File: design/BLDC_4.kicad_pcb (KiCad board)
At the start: 4 copper layers, 38.5 x 65 mm, 127 parts, among them K1 SERVO, P1 HALL/Encoder, P101 CANBUS, P2 SWD, P3 PWR_COMM, P4 IN+, P5 IN-, P6 MOTOR1, P7 MOTOR2, P9 MOTOR3, Q1 IRFS7530, Q2 IRFS7530, Q3 IRFS7530, Q4 IRFS7530, Q5 IRFS7530, Q6 IRFS7530, U1 STM32F40X_LQFP64, U2 TC2117, U3 DRV8302, U401 SN65HVD232, X1 MINI-USB-SHIELD-32005-201, X2 8MHz 10ppm

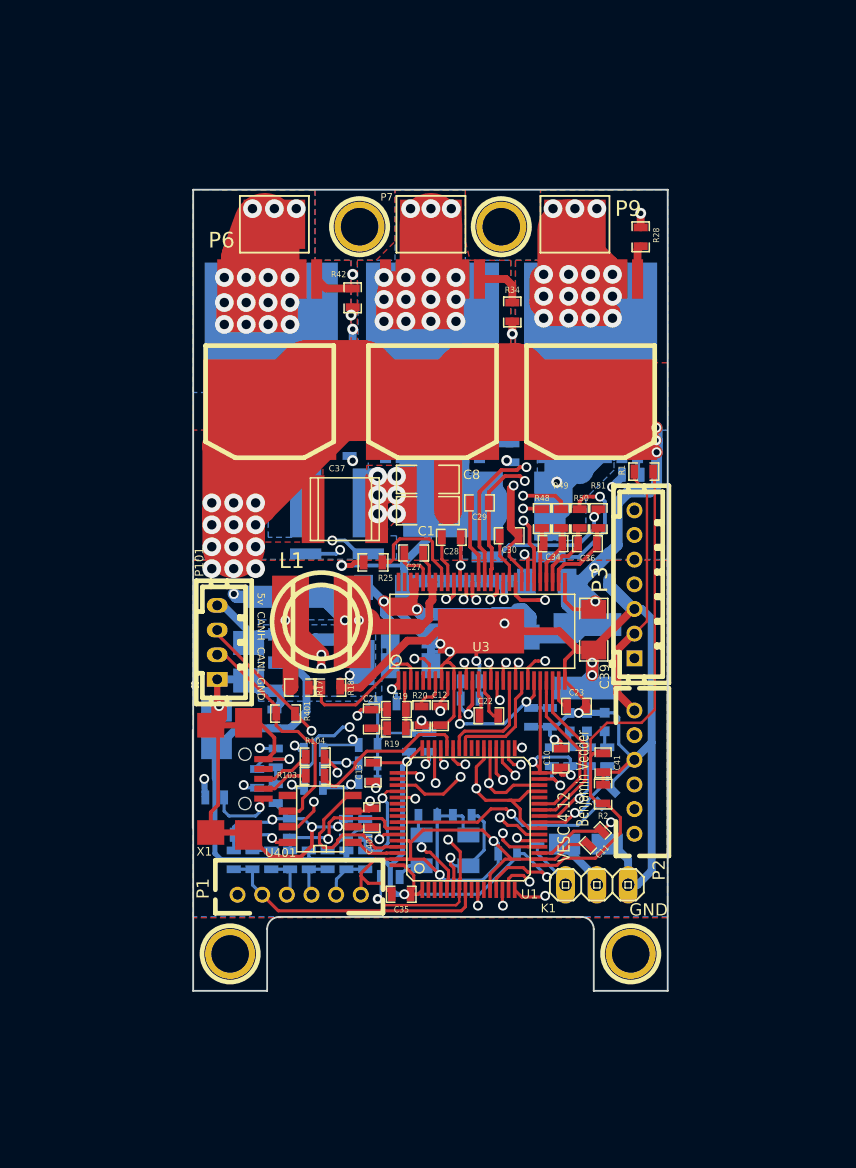
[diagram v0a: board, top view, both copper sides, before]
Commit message: Going to KiCAD 6
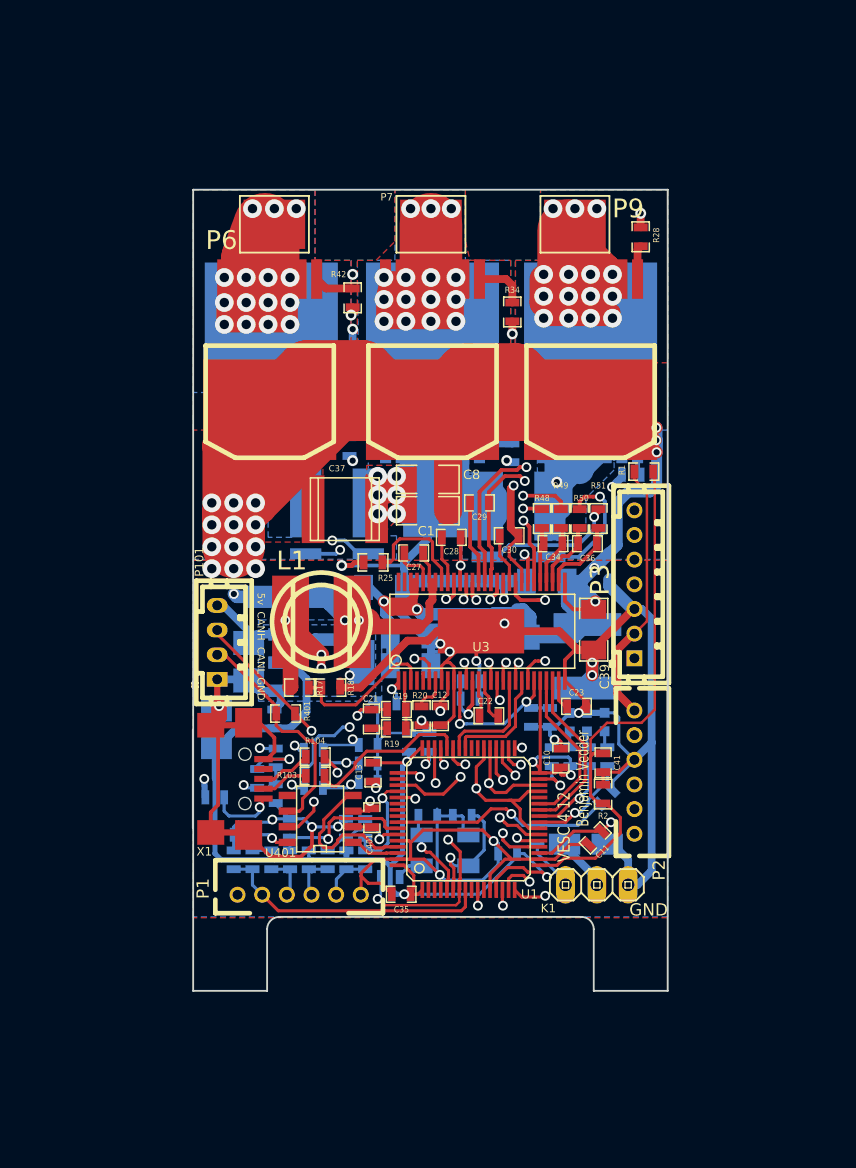
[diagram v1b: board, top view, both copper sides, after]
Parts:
- removed 1PIN (x2): P***, 1pin
- removed 1PIN (x2): P***, Connect:1pin
- removed G***: oshw_silkscreen-back_3mm, oshw_silkscreen-back_3mm
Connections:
- net /Filters/TEMP_IN renamed /Filters/TEMP_MOTOR
- net /MCU/MISO_ADC_EXT2 renamed /MISO_RX_SCL
- net /MCU/RX_SCL_MOSI renamed /RX_SCL_MOSI
- net /MCU/SCK_ADC_EXT renamed /SCK_ADC_EXT
- net /MCU/TX_SDA_NSS renamed /TX_SDA
- P2 pad 6: Net-(P2-Pad6) -> unconnected-(P2-Pad6)
- U1 pad 11: Net-(U1-Pad11) -> unconnected-(U1-Pad11)
- U1 pad 2: Net-(U1-Pad2) -> unconnected-(U1-Pad2)
- U1 pad 28: Net-(U1-Pad28) -> unconnected-(U1-Pad28)
- U1 pad 3: Net-(U1-Pad3) -> unconnected-(U1-Pad3)
- U1 pad 39: Net-(U1-Pad39) -> unconnected-(U1-Pad39)
- U1 pad 4: Net-(U1-Pad4) -> unconnected-(U1-Pad4)
- U1 pad 40: Net-(U1-Pad40) -> unconnected-(U1-Pad40)
- U1 pad 50: Net-(U1-Pad50) -> unconnected-(U1-Pad50)
- U1 pad 54: Net-(U1-Pad54) -> unconnected-(U1-Pad54)
- U1 pad 55: Net-(U1-Pad55) -> unconnected-(U1-Pad55)
- U1 pad 56: Net-(U1-Pad56) -> unconnected-(U1-Pad56)
- U1 pad 9: Net-(U1-Pad9) -> unconnected-(U1-Pad9)
- U3 pad 4: Net-(U3-Pad4) -> unconnected-(U3-Pad4)
- U3 pad 5: Net-(U3-Pad5) -> unconnected-(U3-Pad5)
- U3 pad 55: Net-(U3-Pad55) -> unconnected-(U3-Pad55)
- U3 pad 56: Net-(U3-Pad56) -> unconnected-(U3-Pad56)
- U401 pad 5: Net-(U401-Pad5) -> unconnected-(U401-Pad5)
- X1 pad 4: Net-(X1-Pad4) -> unconnected-(X1-Pad4)
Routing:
- added copper zone on In1.Cu, net /Mosfet driver/H1_VS
- added copper zone on In2.Cu, net /Mosfet driver/H1_VS
- added copper zone on In1.Cu, net /Mosfet driver/H2_VS
- added copper zone on In2.Cu, net /Mosfet driver/H2_VS
- added copper zone on In1.Cu, net /Mosfet driver/H3_VS
- added copper zone on In2.Cu, net /Mosfet driver/H3_VS
- added copper zone on In1.Cu, net GND
- added copper zone on In2.Cu, net GND
- removed copper zone on GND, net /Mosfet driver/H1_VS
- removed copper zone on GND2, net /Mosfet driver/H1_VS
- removed copper zone on GND, net /Mosfet driver/H2_VS
- removed copper zone on GND2, net /Mosfet driver/H2_VS
- removed copper zone on GND, net /Mosfet driver/H3_VS
- removed copper zone on GND2, net /Mosfet driver/H3_VS
- removed copper zone on GND, net GND
- removed copper zone on GND2, net GND
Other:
- net class Default removed

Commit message: Moving to KICAD 6
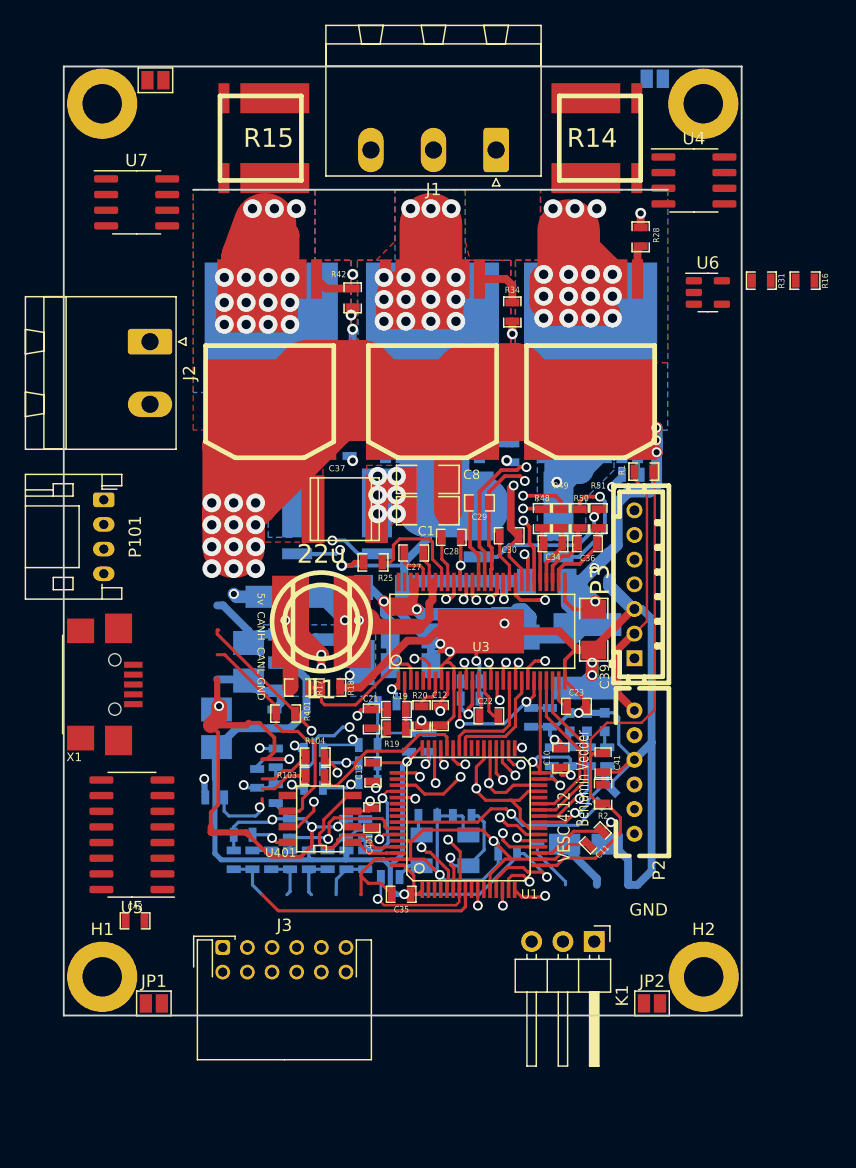
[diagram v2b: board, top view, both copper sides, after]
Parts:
- removed P1: HALL/Encoder, CRF1:MICRO_JST_6
- removed P4: IN+, CRF1:1PAD_4x5mm
- removed P5: IN-, CRF1:1PAD_4x5mm
- removed P6: MOTOR1, CRF1:1PAD_4x5mm
- removed P7: MOTOR2, CRF1:1PAD_4x5mm
- removed P9: MOTOR3, CRF1:1PAD_4x5mm
- added C42: 100n, CRF1:SMD-0603_c, F.Cu at (73.8, 139.3)
- added H1: MountingHole_Pad, MountingHole:MountingHole_3.2mm_M3_ISO7380_Pad, F.Cu at (71.1, 143.9)
- added H2: MountingHole_Pad, MountingHole:MountingHole_3.2mm_M3_ISO7380_Pad, F.Cu at (119.9, 143.9)
- added H3: MountingHole_Pad, MountingHole:MountingHole_3.2mm_M3_ISO7380_Pad, F.Cu at (71.1, 73.0)
- added H4: MountingHole_Pad, MountingHole:MountingHole_3.2mm_M3_ISO7380_Pad, F.Cu at (119.9, 73.0)
- added J1: Conn_01x03, Connector_Phoenix_MSTB:PhoenixContact_MSTBA_2,5_3-G-5,08_1x03_P5.08mm_Horizontal, F.Cu at (103.1, 76.8)
- added J2: Conn_01x02, Connector_Phoenix_MSTB:PhoenixContact_MSTBA_2,5_2-G-5,08_1x02_P5.08mm_Horizontal, F.Cu at (75.0, 92.3)
- added J3: Conn_02x06_Odd_Even, Connector_JST:JST_PHD_S12B-PHDSS_2x06_P2.00mm_Horizontal, F.Cu at (80.9, 141.5)
- added JP1: Jumper_2_Open, Jumper:SolderJumper-2_P1.3mm_Open_Pad1.0x1.5mm, F.Cu at (75.3, 146.0)
- added JP2: Jumper_2_Open, Jumper:SolderJumper-2_P1.3mm_Open_Pad1.0x1.5mm, F.Cu at (115.7, 146.0)
- added JP3: Jumper_2_Open, Jumper:SolderJumper-2_P1.3mm_Open_Pad1.0x1.5mm, F.Cu at (75.4, 71.1)
- added JP4: Jumper_2_Open, Jumper:SolderJumper-2_P1.3mm_Open_Pad1.0x1.5mm, B.Cu at (116.0, 71.0)
- added R14: SHUNT, CRF1:WSLP2726, F.Cu at (113.4, 75.8)
- added R15: SHUNT, CRF1:WSLP2726, F.Cu at (82.1, 75.8)
- added R16: 100R, CRF1:SMD-0603_r, F.Cu at (128.1, 87.4)
- added R31: 100R, CRF1:SMD-0603_r, F.Cu at (124.6, 87.4)
- added U4: INA826AIDR, Package_SO:SOIC-8_3.9x4.9mm_P1.27mm, F.Cu at (119.1, 79.2)
- added U5: AM26LV32xD, Package_SO:SOIC-16_3.9x9.9mm_P1.27mm, F.Cu at (73.5, 132.3)
- added U6: OPA333AIDBVR, Package_TO_SOT_SMD:SOT-23-5, F.Cu at (120.3, 88.3)
- added U7: INA826AIDR, Package_SO:SOIC-8_3.9x4.9mm_P1.27mm, F.Cu at (73.9, 81.0)
- K1: footprint CRF1:pinhead-1X03 -> Connector_PinHeader_2.54mm:PinHeader_1x03_P2.54mm_Horizontal
- P101: footprint JST conn:b4b-ph-kl -> Connector_JST:JST_PH_S4B-PH-K_1x04_P2.00mm_Horizontal
- moved P101 14.8 mm to (71.2, 105.2), turned to -90 degrees
- moved X1 13.0 mm to (72.1, 120.1)
- moved K1 4.61 mm to (111.0, 141.0), turned to -90 degrees
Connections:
- net /Filters/HALL1_IN renamed /HALL_U
- net /Filters/HALL2_IN renamed /HALL_V
- net /Filters/HALL3_IN renamed /HALL_W
- net /Filters/TEMP_MOTOR renamed /RTC+
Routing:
- net +5V: track 115.3 -> 79.6 mm
- net GND: track 398.8 -> 434.5 mm
- net /Mosfet driver/H1_VS: track 150.6 -> 162.0 mm, vias 17 -> 18
- net /Mosfet driver/SH2_B: track 11.4 -> 0.00 mm, vias 1 -> 0
- removed copper zone on B.Cu, net GND
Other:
- board size 38.5 x 65 mm -> 55 x 77 mm

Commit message: STM pins connected
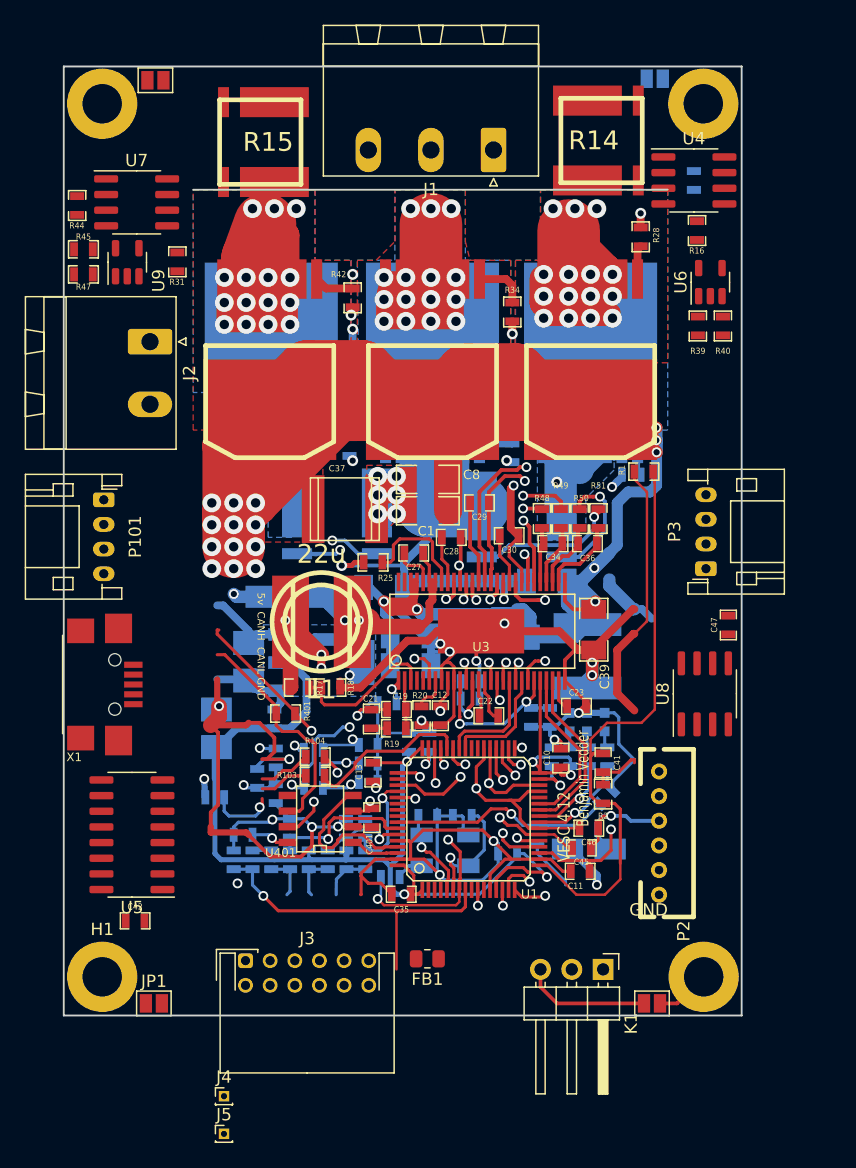
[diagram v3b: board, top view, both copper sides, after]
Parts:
- added C45: 10n, CRF1:SMD-0603_c, F.Cu at (110.0, 133.4)
- added C46: 10n, CRF1:SMD-0603_c, F.Cu at (110.6, 131.8)
- added C47: 100n, CRF1:SMD-0603_c, F.Cu at (121.9, 115.3)
- added FB1: FerriteBead, Resistor_SMD:R_0805_2012Metric, F.Cu at (97.5, 142.4)
- added J4: Conn_01x01_Pin, Connector_PinHeader_1.00mm:PinHeader_1x01_P1.00mm_Vertical, F.Cu at (81.0, 153.6)
- added J5: Conn_01x01_Pin, Connector_PinHeader_1.00mm:PinHeader_1x01_P1.00mm_Vertical, F.Cu at (81.0, 156.6)
- added R39: 39k, CRF1:SMD-0603_r, F.Cu at (119.4, 91.1)
- added R40: 39k, CRF1:SMD-0603_r, F.Cu at (121.5, 91.1)
- added R41: 39k, CRF1:SMD-0603_r, B.Cu at (119.1, 79.2)
- added R44: 39k, CRF1:SMD-0603_r, F.Cu at (69.1, 81.3)
- added R45: 39k, CRF1:SMD-0603_r, F.Cu at (69.6, 84.8)
- added R47: 39k, CRF1:SMD-0603_r, F.Cu at (69.6, 86.9)
- added U8: MAX485ED, Package_SO:SOIC-8_3.9x4.9mm_P1.27mm, F.Cu at (120.0, 120.9)
- added U9: OPA333AIDBVR, Package_TO_SOT_SMD:SOT-23-5, F.Cu at (73.2, 85.9)
- P3: footprint CRF1:b7b-ph-kl -> Connector_JST:JST_PH_S4B-PH-K_1x04_P2.00mm_Horizontal
- moved R31 47.4 mm to (77.2, 85.9), turned to -90 degrees
- moved R16 9.66 mm to (119.4, 83.3), turned to -90 degrees
- moved P3 5.94 mm to (120.1, 110.7)
- moved P2 5.34 mm to (116.3, 132.2)
- moved C11 2.98 mm to (109.9, 135.3), turned to 0 degrees
- moved K1 2.37 mm to (111.8, 143.3)
- moved J3 2.13 mm to (82.7, 142.6)
- moved U6 0.87 mm to (120.5, 87.5), turned to 90 degrees
- moved D5 0.47 mm to (110.6, 133.5)
- moved R15 0.32 mm to (82.0, 76.1)
- moved R53 0.25 mm to (105.2, 108.7)
- moved R14 0.23 mm to (113.5, 76.0)
- moved J1 0.21 mm to (102.9, 76.8)
- turned JP2 to 180 degrees
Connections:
- net /ENC_A+ renamed /Encoder/ENC_A+
- net /ENC_A- renamed /Encoder/ENC_A-
- net /ENC_B+ renamed /Encoder/ENC_B+
- net /ENC_B- renamed /Encoder/ENC_B-
- net /HALL_U renamed /Filters/HALL1_IN
- net /HALL_V renamed /Filters/HALL2_IN
- net /HALL_W renamed /Filters/HALL3_IN
- net /RTC+ renamed /Filters/TEMP_MOTOR
- J3 pad 11: +5V -> Net-(J3-Pin_11)
- P3 pad 2: VCC -> Net-(P3-Pin_2)
- P3 pad 3: GND -> Net-(P3-Pin_3)
- P3 pad 4: /SCK_ADC_EXT -> GND
- R16 pad 2: /Power MOSFETS/IPH_1 -> /MCU/IPH_1
- R31 pad 2: /Power MOSFETS/IPH_2 -> /MCU/IPH_3
- U1 pad 11: unconnected-(U1-Pad11) -> /MCU/DE_485
- U1 pad 20: /TX_SDA -> /MCU/DAC1
- U1 pad 21: /SCK_ADC_EXT -> /MCU/DAC2
- U1 pad 22: /MISO_RX_SCL -> /MCU/IPH_1
- U1 pad 23: /RX_SCL_MOSI -> /MCU/IPH_3
- U1 pad 29: /RX_SCL_MOSI -> /MCU/TX_485
- U1 pad 30: /TX_SDA -> /MCU/RX_485
- U1 pad 37: /TX_SDA -> /Encoder/ENC_A
- U1 pad 38: /RX_SCL_MOSI -> /Encoder/ENC_B
- U1 pad 39: unconnected-(U1-Pad39) -> /Encoder/ENC_0
- U1 pad 9: unconnected-(U1-Pad9) -> /MCU/RE_485
- U4 pad 2: unconnected-(U4-Pad2) -> Net-(R41-Pad1)
- U4 pad 3: unconnected-(U4-Pad3) -> Net-(R41-Pad2)
- U4 pad 5: unconnected-(U4-Pad5) -> GND
- U4 pad 6: unconnected-(U4-Pad6) -> Net-(U4-Ref)
- U4 pad 8: unconnected-(U4-Pad8) -> +5V
- U6 pad 1: unconnected-(U6-Pad1) -> Net-(U4-Ref)
- U6 pad 2: unconnected-(U6-Pad2) -> GND
- U6 pad 3: unconnected-(U6-Pad3) -> Net-(U6-+)
- U6 pad 4: unconnected-(U6-Pad4) -> Net-(U4-Ref)
- U6 pad 5: unconnected-(U6-Pad5) -> VCC
- U7 pad 2: unconnected-(U7-Pad2) -> Net-(R44-Pad1)
- U7 pad 3: unconnected-(U7-Pad3) -> Net-(R44-Pad2)
- U7 pad 5: unconnected-(U7-Pad5) -> GND
- U7 pad 6: unconnected-(U7-Pad6) -> Net-(U7-Ref)
- U7 pad 8: unconnected-(U7-Pad8) -> +5V
- X2 pad 4: (no net) -> GND
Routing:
- net (no net): track 0.00 -> 88.4 mm
- net /TX_SDA: track 47.1 -> 0.00 mm, vias 2 -> 0
- net GND: track 434.5 -> 390.7 mm, vias 27 -> 28
- net /RX_SCL_MOSI: track 41.6 -> 0.00 mm, vias 1 -> 0
- net /MCU/IPH_1: track 0.00 -> 39.1 mm, vias 0 -> 1
- net /MISO_RX_SCL: track 36.0 -> 0.00 mm, vias 1 -> 0
- net /SCK_ADC_EXT: track 26.4 -> 0.00 mm, vias 1 -> 0
- net /MCU/DAC2: track 0.00 -> 26.4 mm, vias 0 -> 1
- net +5V: track 79.6 -> 92.5 mm, vias 4 -> 6
- net /Mosfet driver/SH2_B: track 0.00 -> 12.1 mm, vias 0 -> 1
- net /Mosfet driver/H1_VS: track 162.0 -> 150.4 mm, vias 18 -> 17
- net /Filters/TEMP_MOTOR: track 22.4 -> 27.3 mm, vias 0 -> 1
- net /MCU/ADC_TEMP: track 44.0 -> 48.6 mm
- net Net-(JP2-A): track 0.00 -> 4.44 mm
- net /MCU/IPH_3: track 0.00 -> 2.85 mm
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
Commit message: Última versão de hoje
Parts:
- added J6: Conn_02x06_Odd_Even, Connector_JST:JST_PH_S2B-PH-K_1x02_P2.00mm_Horizontal, F.Cu at (80.0, 144.8)
- added REF**: R_2512_6332Metric, Resistor_SMD:R_2512_6332Metric, F.Cu at (111.5, 76.2)
- P2: footprint CRF1:MICRO_JST_6 -> Connector_JST:JST_PH_B6B-PH-K_1x06_P2.00mm_Vertical
- moved J5 32.8 mm to (108.8, 139.2)
- moved J4 23.5 mm to (99.6, 139.2)
- moved P101 13.7 mm to (71.3, 91.5)
- moved J2 12.3 mm to (76.2, 104.5)
- moved P2 4.95 mm to (116.3, 127.3)
- moved FB1 4.74 mm to (102.2, 142.2)
- moved J3 4.42 mm to (87.2, 142.2)
- moved JP4 1.15 mm to (114.8, 71.1)
- moved C11 0.97 mm to (109.9, 136.3)
- moved JP2 0.73 mm to (115.3, 145.4), turned to 90 degrees
- moved JP1 0.55 mm to (75.8, 145.8)
- moved R1 0.52 mm to (115.2, 103.4)
- moved JP3 0.51 mm to (75.9, 71.1)
- moved K1 0.38 mm to (111.8, 142.9)
- moved C31 0.28 mm to (103.8, 134.0)
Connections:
- C3 pad 2: /MCU/SERVO -> GND
- R39 pad 2: Net-(U6-+) -> GND
- R40 pad 1: Net-(U6-+) -> GND
- R5 pad 1: /MCU/SERVO -> GND
- U1 pad 11: /MCU/DE_485 -> /MCU/RE_485
- U1 pad 57: /MCU/SERVO -> GND
- U1 pad 9: /MCU/RE_485 -> /MCU/DE_485
- U6 pad 3: Net-(U6-+) -> GND
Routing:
- net GND: track 390.7 -> 596.3 mm, vias 28 -> 34
- net +5V: track 92.5 -> 261.3 mm, vias 6 -> 13
- net /MCU/IPH_3: track 2.85 -> 106.9 mm, vias 0 -> 2
- net (no net): track 88.4 -> 0.00 mm
- net VCC: track 186.2 -> 268.6 mm, vias 9 -> 11
- net /Encoder/ENC_0: track 0.00 -> 58.9 mm, vias 0 -> 2
- net /Encoder/ENC_B: track 0.00 -> 52.1 mm, vias 0 -> 2
- net /Encoder/ENC_A: track 0.00 -> 46.3 mm
- net /MCU/DE_485: track 0.00 -> 36.9 mm
- net /MCU/TX_485: track 0.00 -> 35.7 mm, vias 1 -> 3
- net /MCU/RE_485: track 0.00 -> 33.2 mm
- net /CAN bus transceiver/CANL: track 19.0 -> 50.1 mm
- net /MCU/RX_485: track 0.00 -> 29.1 mm, vias 0 -> 3
- net /CAN bus transceiver/CANH: track 21.2 -> 47.8 mm
- net V_SUPPLY: track 290.3 -> 315.9 mm, vias 20 -> 26
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- added copper zone on F.Cu, net /Power MOSFETS/PHASE_1
- added copper zone on F.Cu, net /Power MOSFETS/PHASE_3
- added copper zone on In1.Cu, net V_SUPPLY
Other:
- outline, holes or cut-outs redrawn
- board text removed: "Benjamin Vedder"
- board text removed: "VESC 4.12"
- board text removed: "vedder.se"
